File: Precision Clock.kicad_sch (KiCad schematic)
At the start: 0 parts

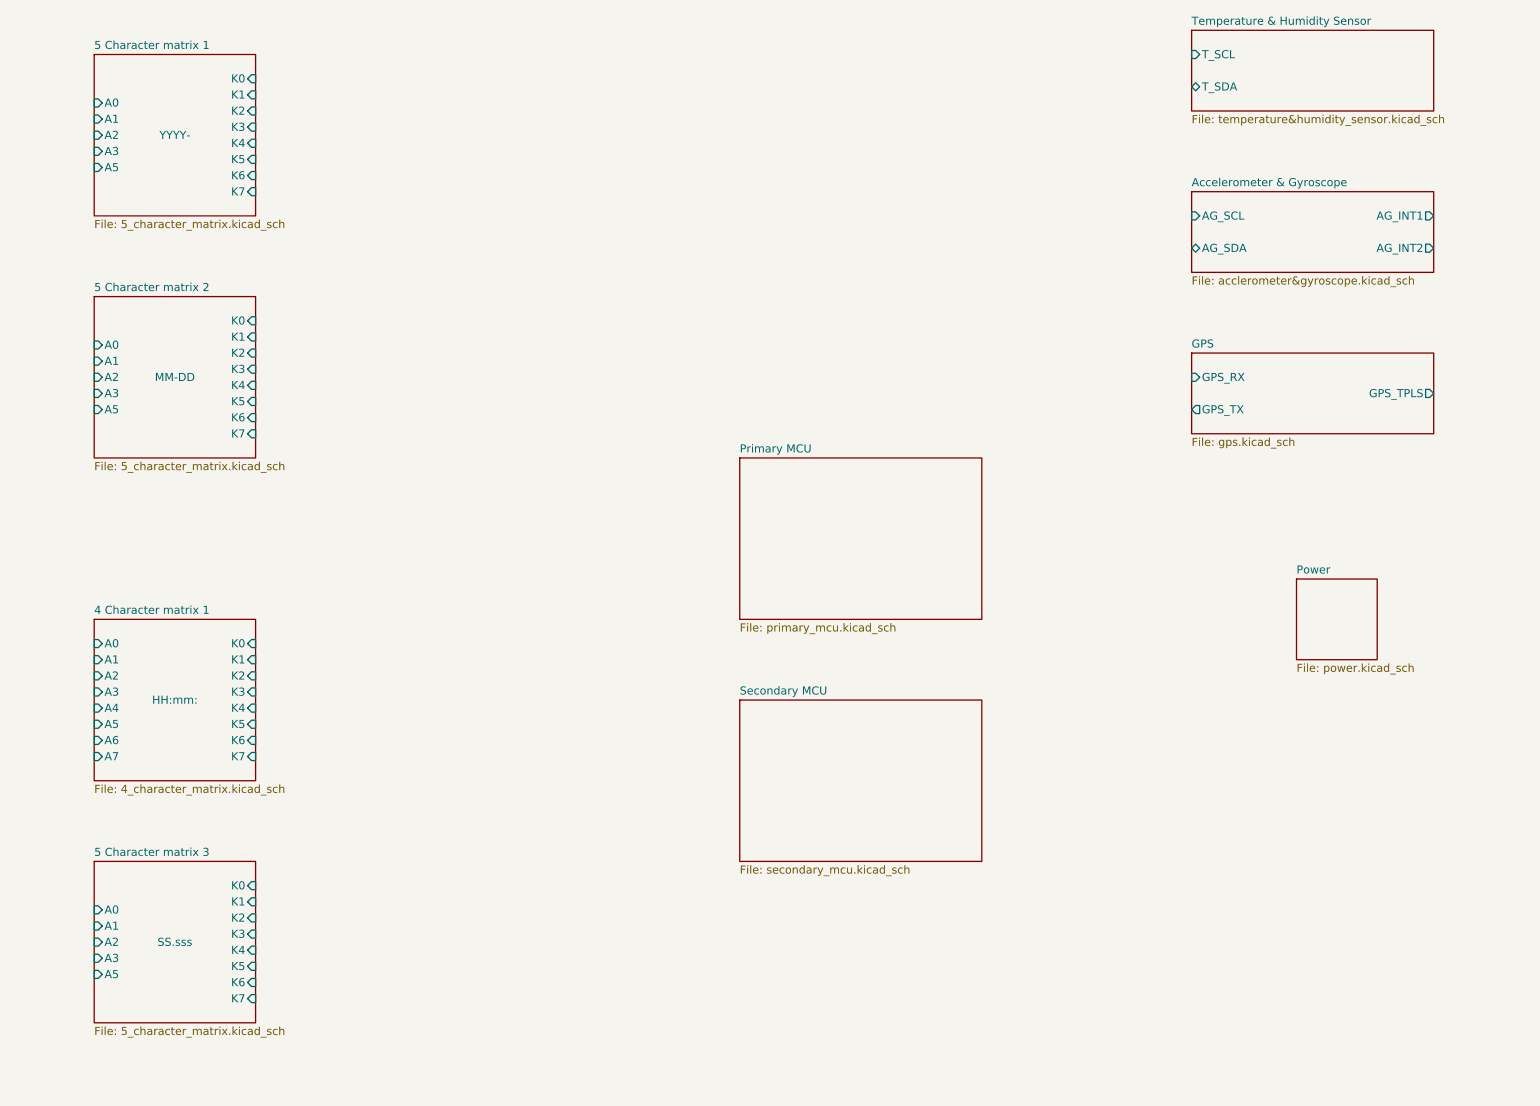
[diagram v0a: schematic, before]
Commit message: power circuit added
- addition of power circuit
- added bypassing circuit
- new formatting of the schematic
- root schematic updated
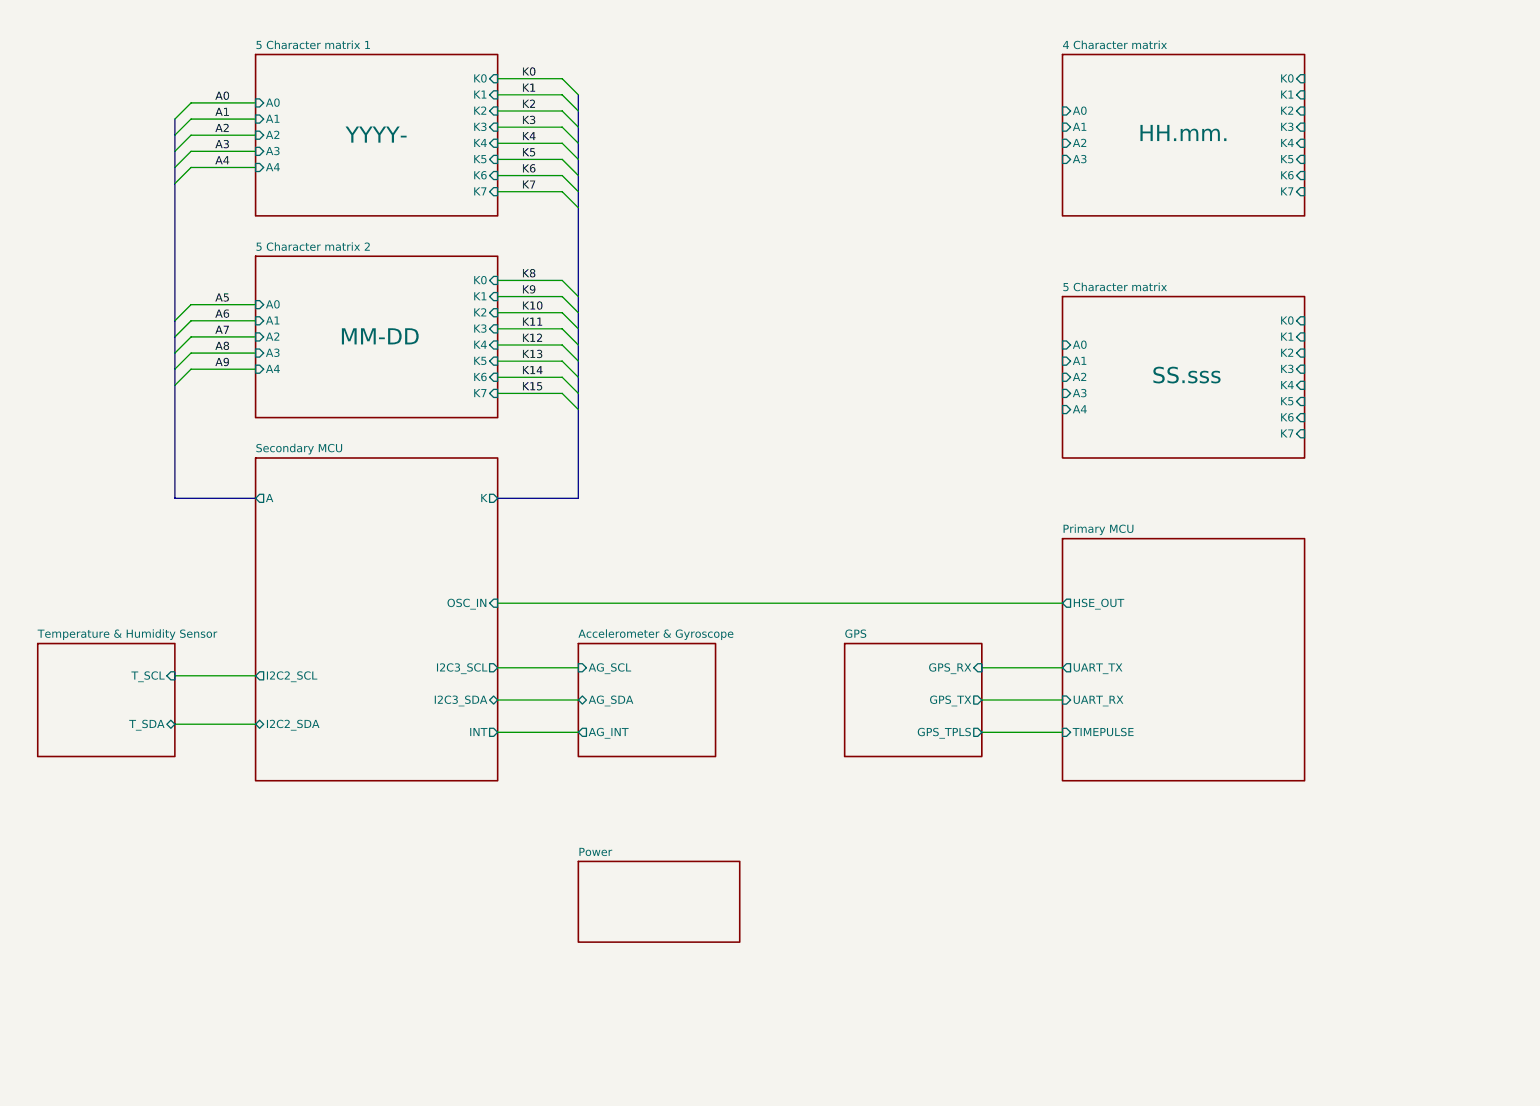
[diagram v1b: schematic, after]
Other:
- sheet 4 Character matrix 1 renamed 4 Character matrix
- sheet 5 Character matrix 3 renamed 5 Character matrix
- sheet 4 Character matrix: file 4_character_matrix.kicad_sch -> 4L_character_matrix.kicad_sch
- sheet 4 Character matrix ports: added none; removed A4, A5, A6, A7
- sheet 5 Character matrix: file 5_character_matrix.kicad_sch -> 5L_character_matrix.kicad_sch
- sheet 5 Character matrix ports: added A4; removed A5
- sheet 5 Character matrix 1: file 5_character_matrix.kicad_sch -> 5U_character_matrix.kicad_sch
- sheet 5 Character matrix 1 ports: added A4; removed A5
- sheet 5 Character matrix 2: file 5_character_matrix.kicad_sch -> 5U_character_matrix.kicad_sch
- sheet 5 Character matrix 2 ports: added A4; removed A5
- sheet Accelerometer & Gyroscope ports: added AG_INT; removed AG_INT1, AG_INT2
- sheet Primary MCU ports: added HSE_OUT, TIMEPULSE, UART_RX, UART_TX; removed none
- sheet Secondary MCU ports: added A, I2C2_SCL, I2C2_SDA, I2C3_SCL, I2C3_SDA, INT, K, OSC_IN; removed none

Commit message: addition of bus
- cleaned up the structure of the schematic.
- addition of the colon
- root schematic improvements
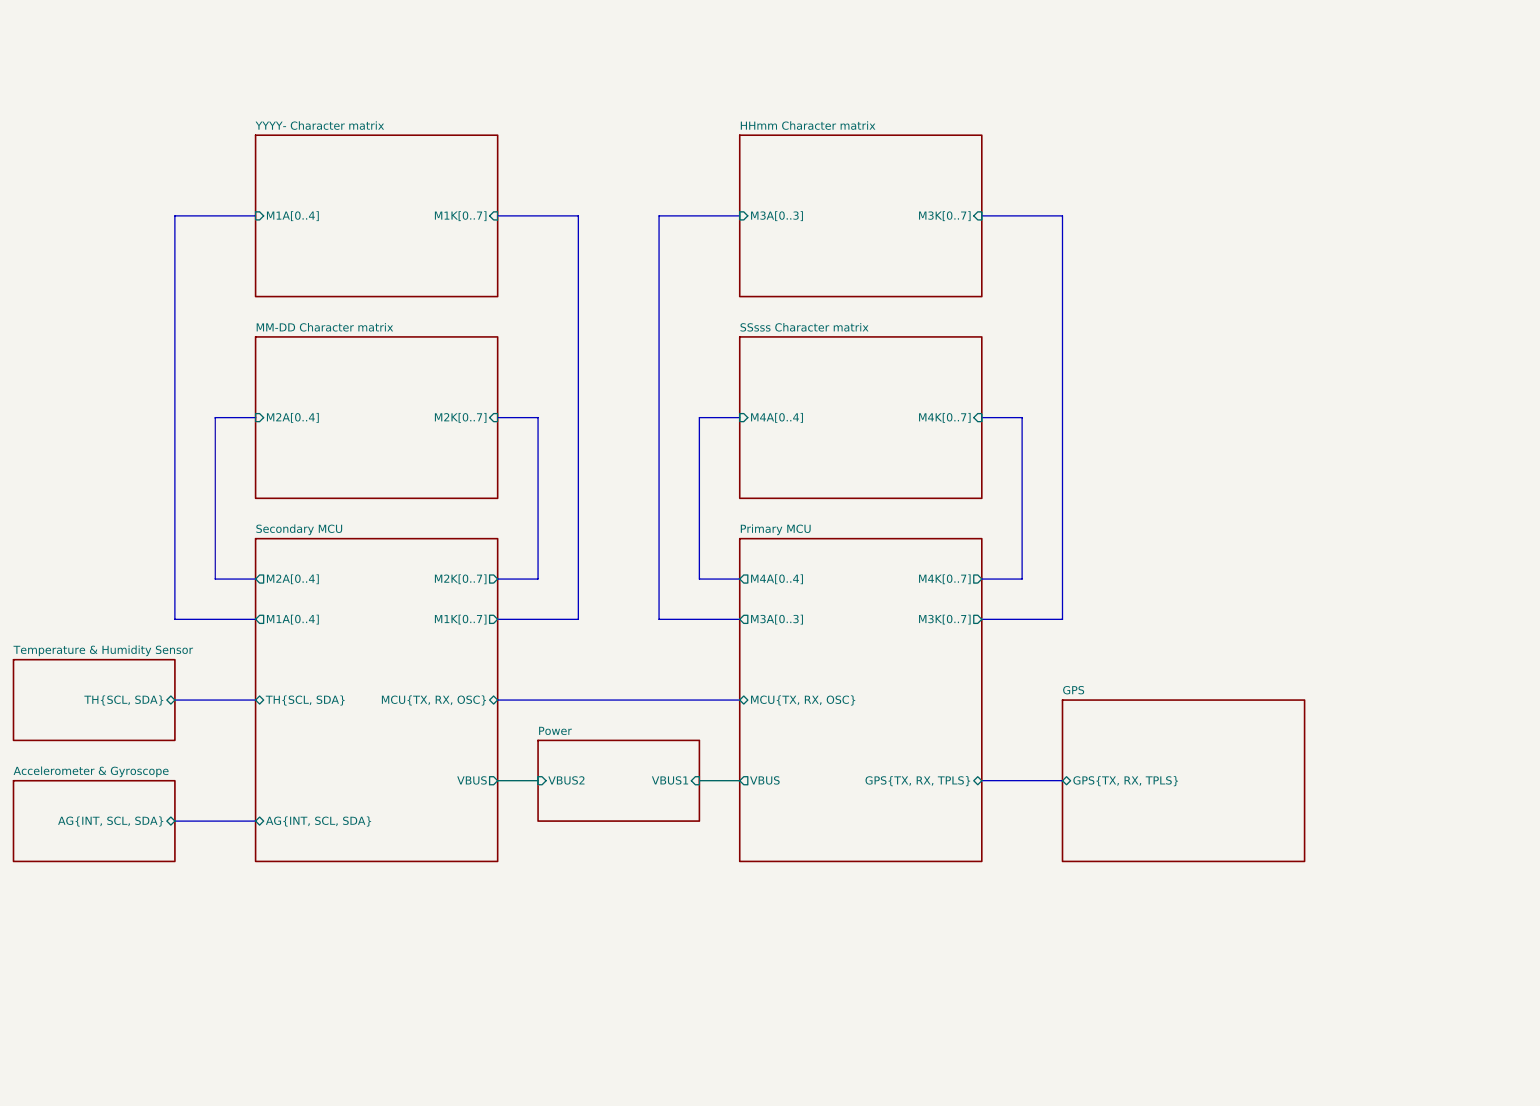
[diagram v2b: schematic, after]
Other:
- sheet 4 Character matrix renamed HHmm Character matrix
- sheet 5 Character matrix renamed SSsss Character matrix
- sheet 5 Character matrix 1 renamed YYYY- Character matrix
- sheet 5 Character matrix 2 renamed MM-DD Character matrix
- sheet Accelerometer & Gyroscope ports: added AG{INT, SCL, SDA}; removed AG_INT, AG_SCL, AG_SDA
- sheet GPS ports: added GPS{TX, RX, TPLS}; removed GPS_RX, GPS_TPLS, GPS_TX
- sheet HHmm Character matrix: file 4L_character_matrix.kicad_sch -> HHmm_character_matrix.kicad_sch
- sheet HHmm Character matrix ports: added M3A[0..3], M3K[0..7]; removed A0, A1, A2, A3, K0, K1, K2, K3, K4, K5, K6, K7
- sheet MM-DD Character matrix: file 5U_character_matrix.kicad_sch -> MM-DD_character_matrix.kicad_sch
- sheet MM-DD Character matrix ports: added M2A[0..4], M2K[0..7]; removed A0, A1, A2, A3, A4, K0, K1, K2, K3, K4, K5, K6, K7
- sheet Power ports: added VBUS1, VBUS2; removed none
- sheet Primary MCU ports: added GPS{TX, RX, TPLS}, M3A[0..3], M3K[0..7], M4A[0..4], M4K[0..7], MCU{TX, RX, OSC}, VBUS; removed HSE_OUT, TIMEPULSE, UART_RX, UART_TX
- sheet SSsss Character matrix: file 5L_character_matrix.kicad_sch -> SSsss_character_matrix.kicad_sch
- sheet SSsss Character matrix ports: added M4A[0..4], M4K[0..7]; removed A0, A1, A2, A3, A4, K0, K1, K2, K3, K4, K5, K6, K7
- sheet Secondary MCU ports: added AG{INT, SCL, SDA}, M1A[0..4], M1K[0..7], M2A[0..4], M2K[0..7], MCU{TX, RX, OSC}, TH{SCL, SDA}, VBUS; removed A, I2C2_SCL, I2C2_SDA, I2C3_SCL, I2C3_SDA, INT, K, OSC_IN
- sheet Temperature & Humidity Sensor ports: added TH{SCL, SDA}; removed T_SCL, T_SDA
- sheet YYYY- Character matrix: file 5U_character_matrix.kicad_sch -> YYYY-_character_matrix.kicad_sch
- sheet YYYY- Character matrix ports: added M1A[0..4], M1K[0..7]; removed A0, A1, A2, A3, A4, K0, K1, K2, K3, K4, K5, K6, K7

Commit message: voltage regulation changes
- ambient light sensor addition
- colon control
- brightness control through regulators
- added test points
- MCU pinout changes
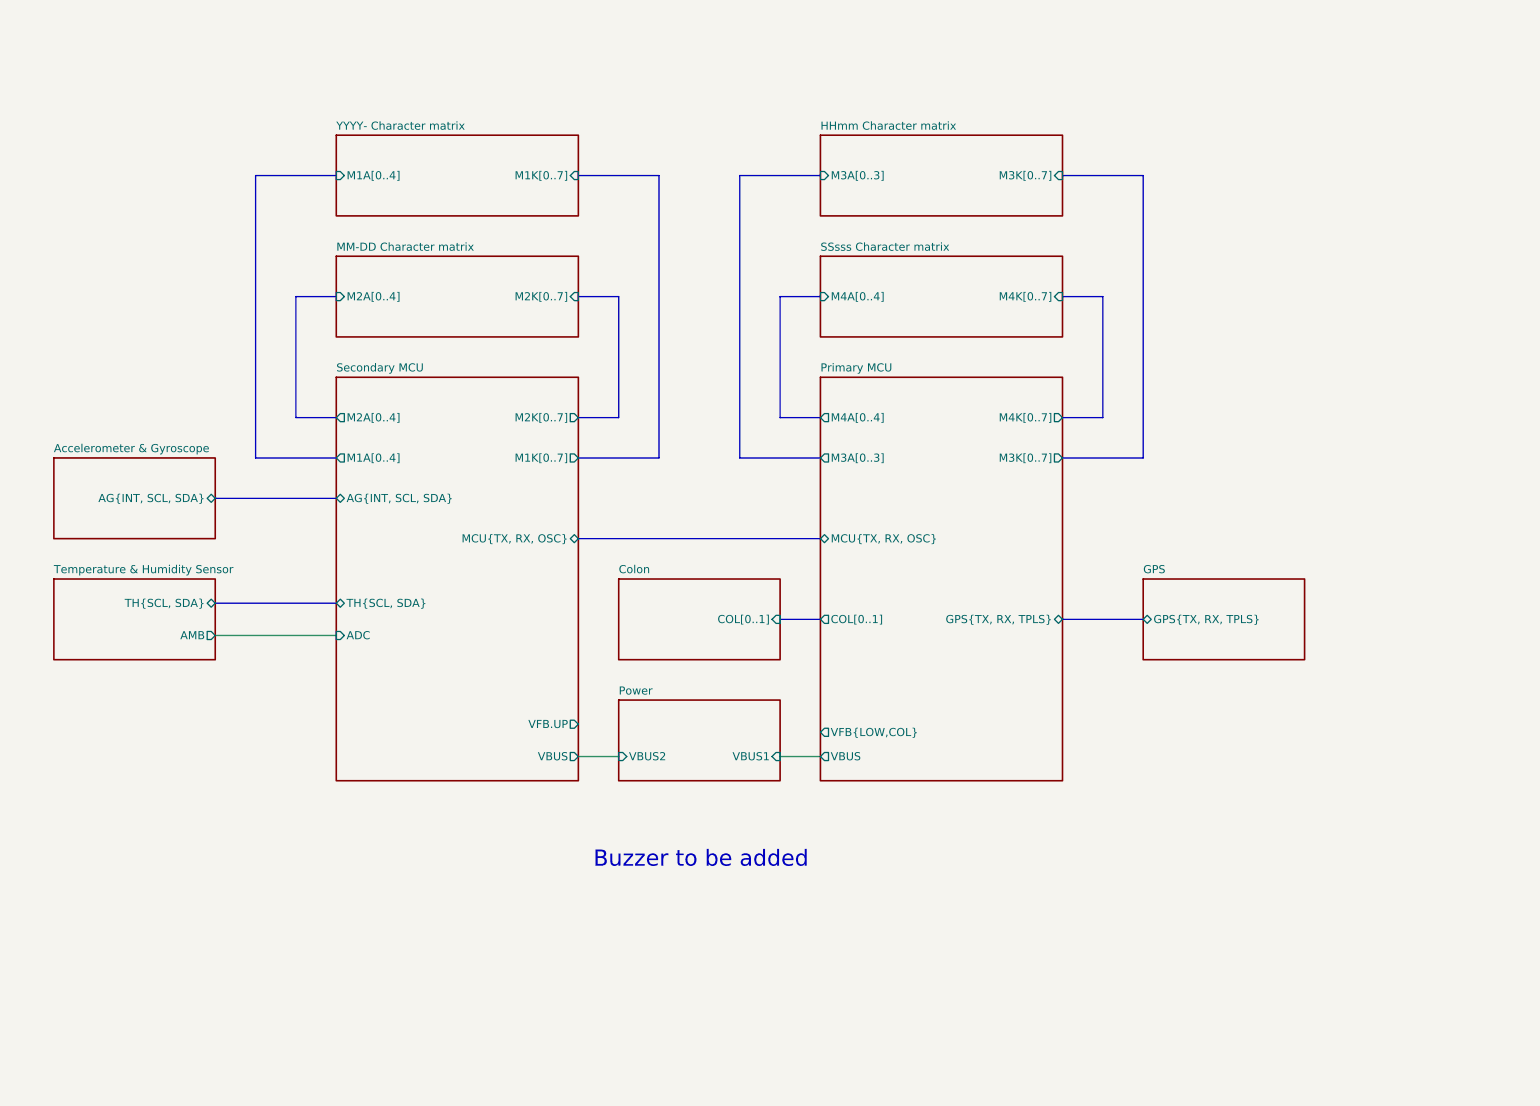
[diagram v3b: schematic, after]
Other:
- added sheet Colon (colon.kicad_sch)
- sheet Primary MCU ports: added COL[0..1], VFB{LOW,COL}; removed none
- sheet Secondary MCU ports: added ADC, VFB.UP; removed none
- sheet Temperature & Humidity Sensor ports: added AMB; removed none
- note added: "Buzzer to be added"

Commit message: buzzer addition
- reordering
- test point addition
- ferrite beads on both the MCUs
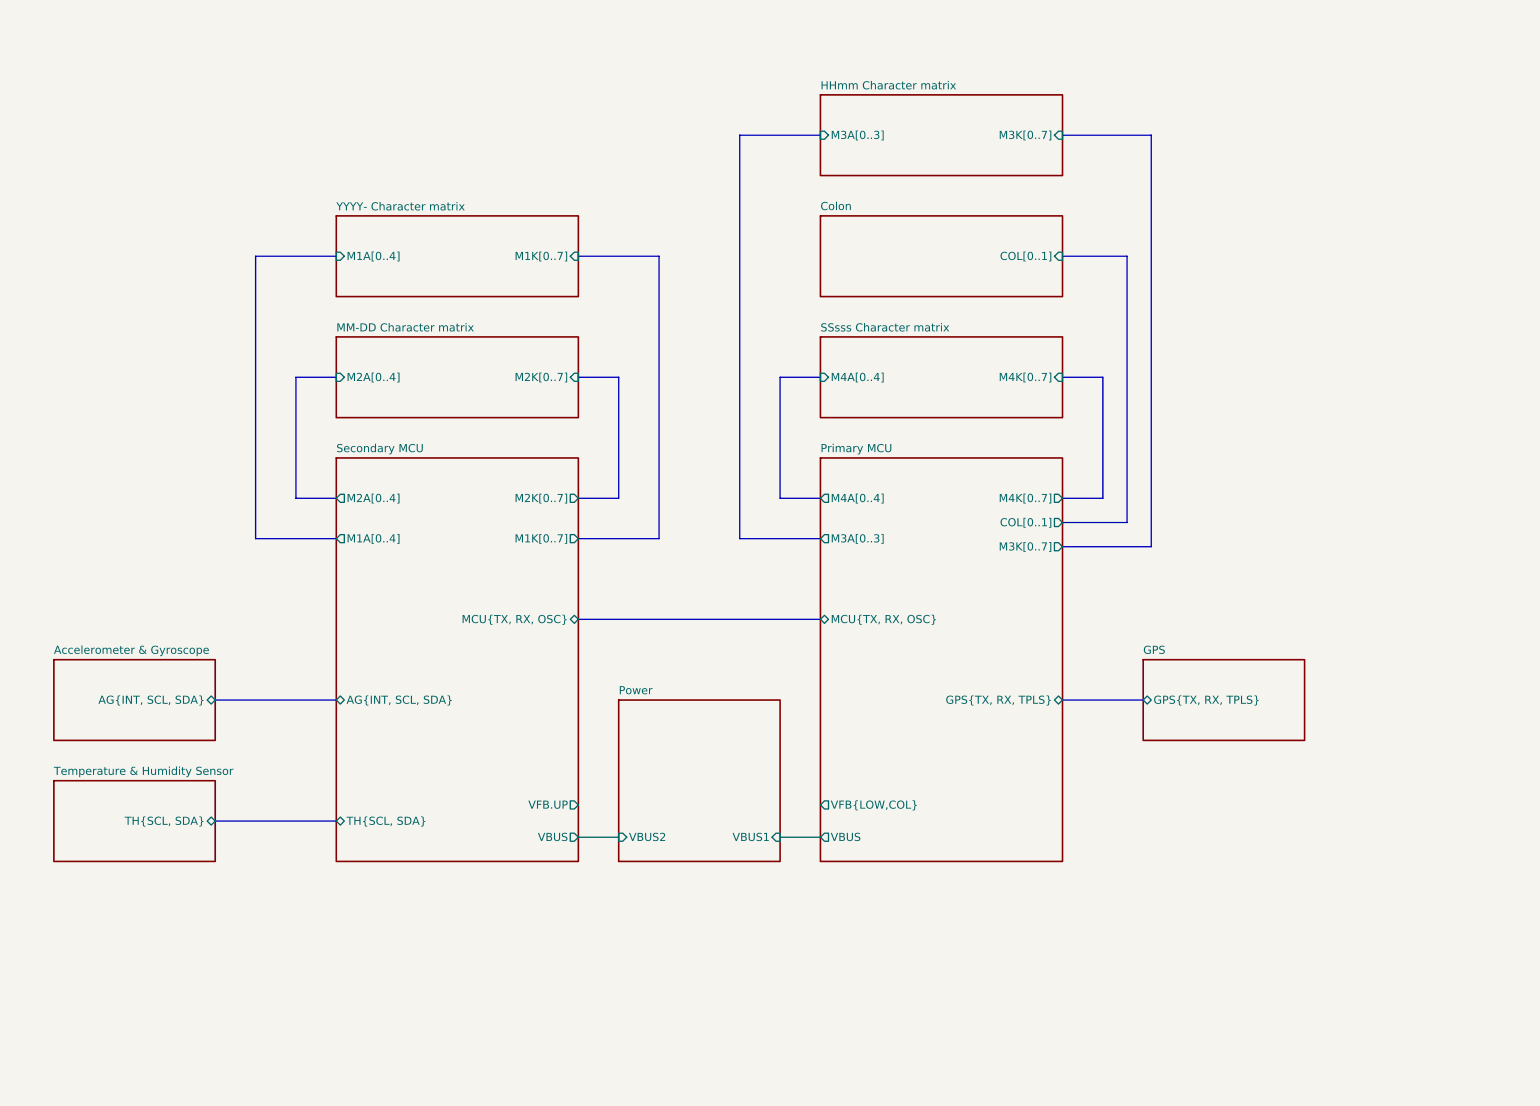
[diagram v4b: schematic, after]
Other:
- sheet Secondary MCU ports: added none; removed ADC
- sheet Temperature & Humidity Sensor ports: added none; removed AMB
- note removed: "Buzzer to be added"

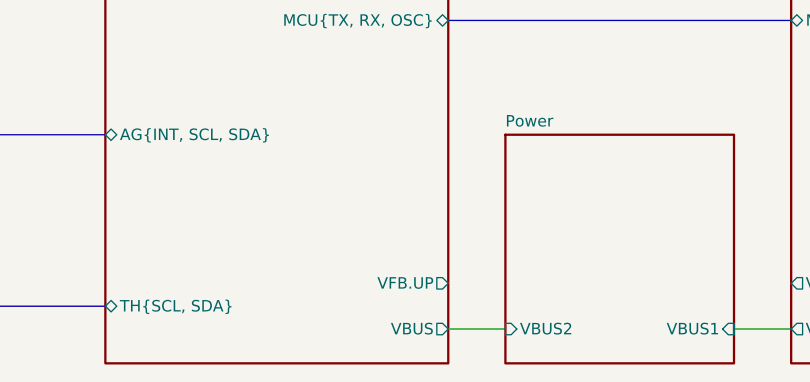
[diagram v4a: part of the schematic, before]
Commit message: Buzzer driver added - replacement of photoresistor to a variable resistor - added button - general formatting
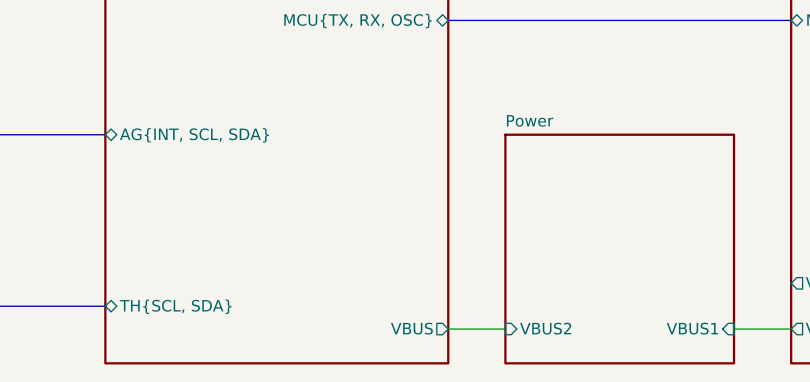
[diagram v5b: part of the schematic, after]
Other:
- sheet Secondary MCU ports: added none; removed VFB.UP
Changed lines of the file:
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@@
-			)
-		)
-		(pin "VFB.UP" output
-			(at 127 143.51 0)
-			(effects
-				(font
-					(size 1.27 1.27)
-				)
-				(justify right)
 			)
 		)
